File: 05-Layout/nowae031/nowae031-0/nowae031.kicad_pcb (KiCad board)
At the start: 2 copper layers, 50 x 89.2 mm, 75 parts, among them P101 COMM, P102 SUPPLY, U101 TCA9554PWR, U102 TCA9554PWR

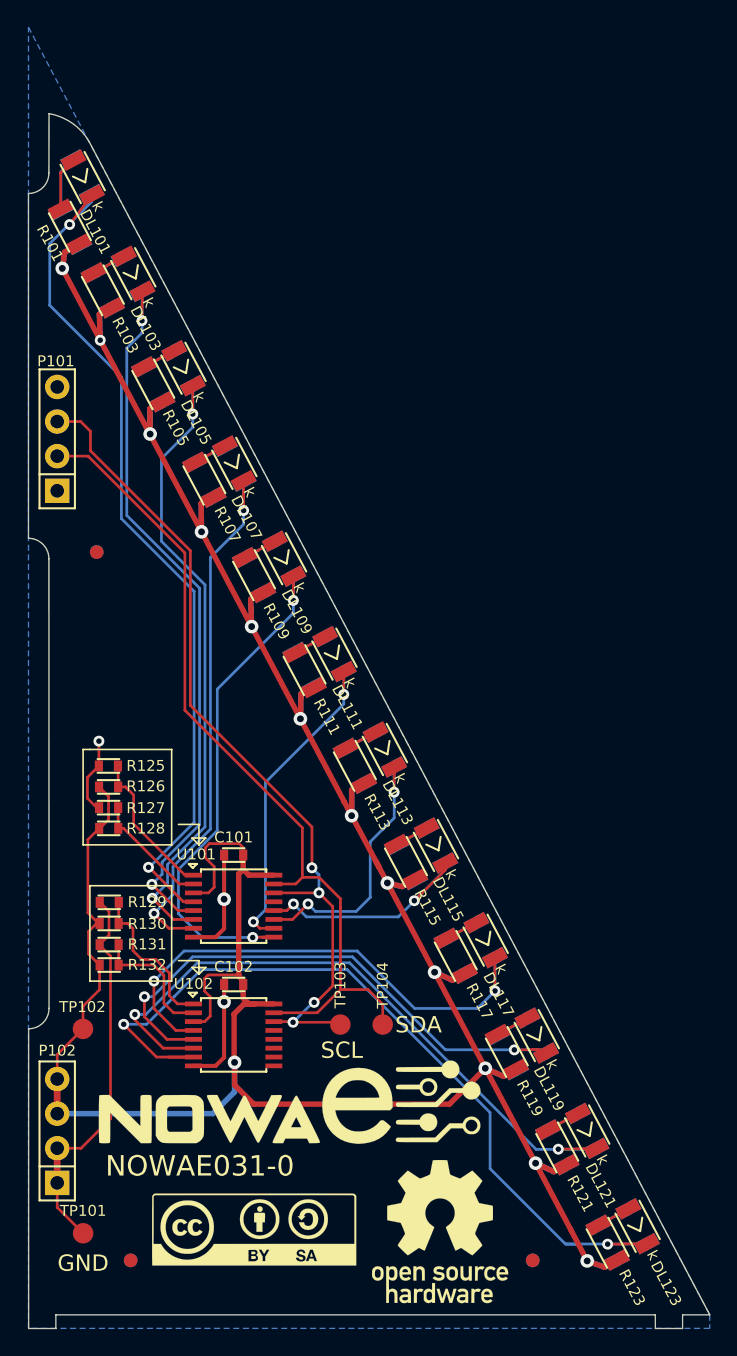
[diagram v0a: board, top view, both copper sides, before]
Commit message: Fixed connector versus NOWAE029 and generated new gerber files.
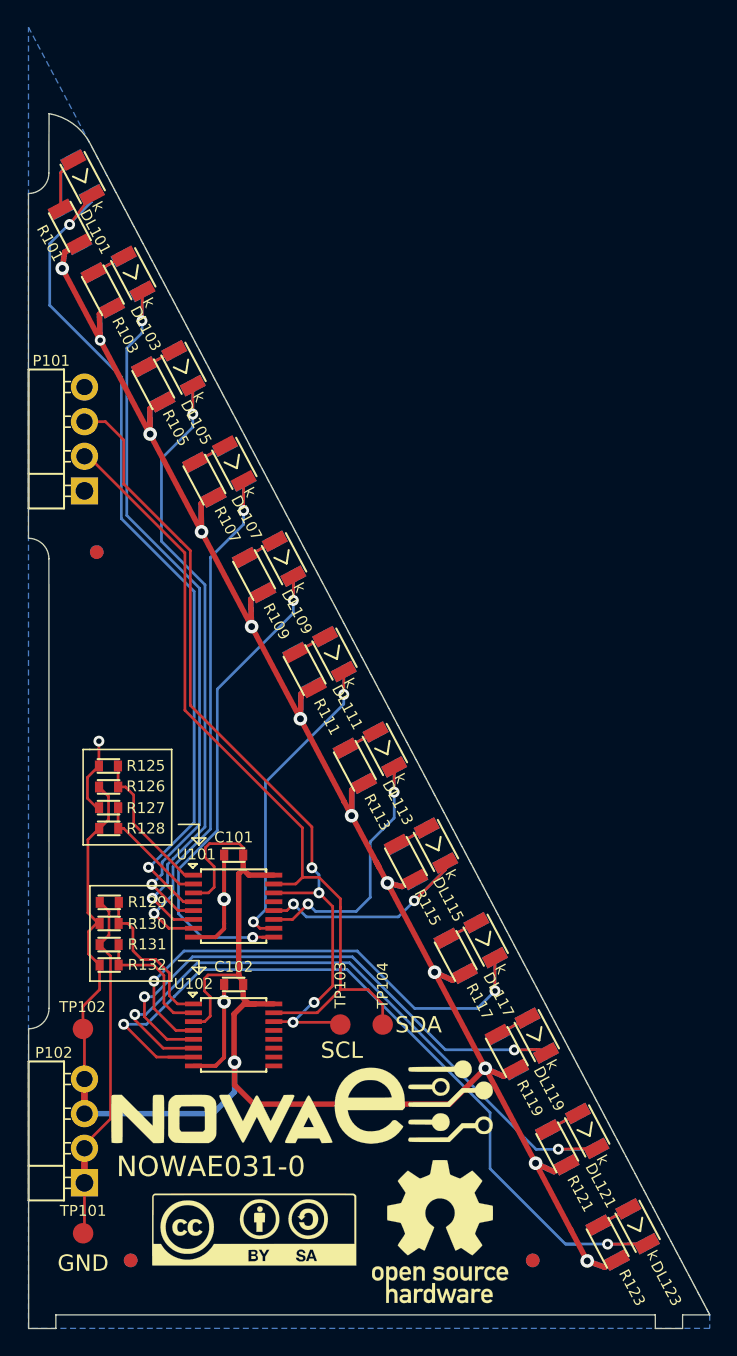
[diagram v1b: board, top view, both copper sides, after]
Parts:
- P101, P102: footprint CONNECTOR:CONN-STRIP-4x1-2.54 -> CONNECTOR:CONN-STRIP-4x1-2.54-ANGLED
- moved P101 2.00 mm to (104.1, 64.7)
- moved P102 2.00 mm to (104.1, 115.5)
- moved G*** 0.91 mm to (120.1, 113.4)
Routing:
- net +3.3V: track 252.4 -> 249.6 mm
- net GND: track 50.4 -> 47.9 mm
- net /BRANCH_SDA: track 62.7 -> 60.5 mm
- net /BRANCH_SCL: track 63.6 -> 62.2 mm
